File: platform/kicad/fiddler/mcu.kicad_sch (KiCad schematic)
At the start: 9 parts, among them SW1 SW_Push, SW2 SW_Push, U1 ESP32-WROOM-32E

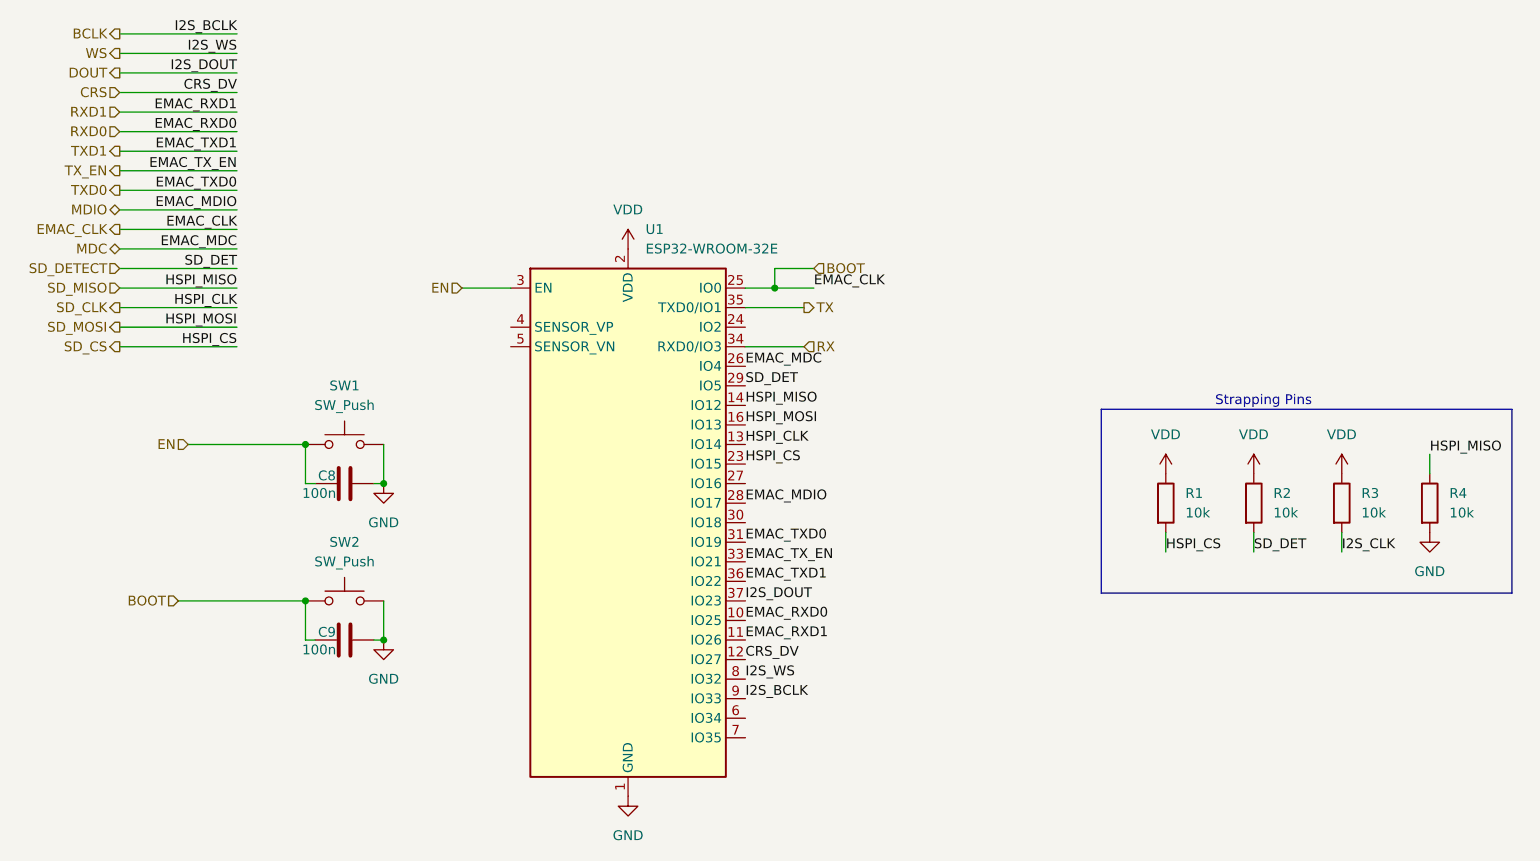
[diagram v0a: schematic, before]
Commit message: Fiddler Ray Speaker: Complete first revision
This change completes the first iteration schematic and layout for the fiddler ray speaker PCB.
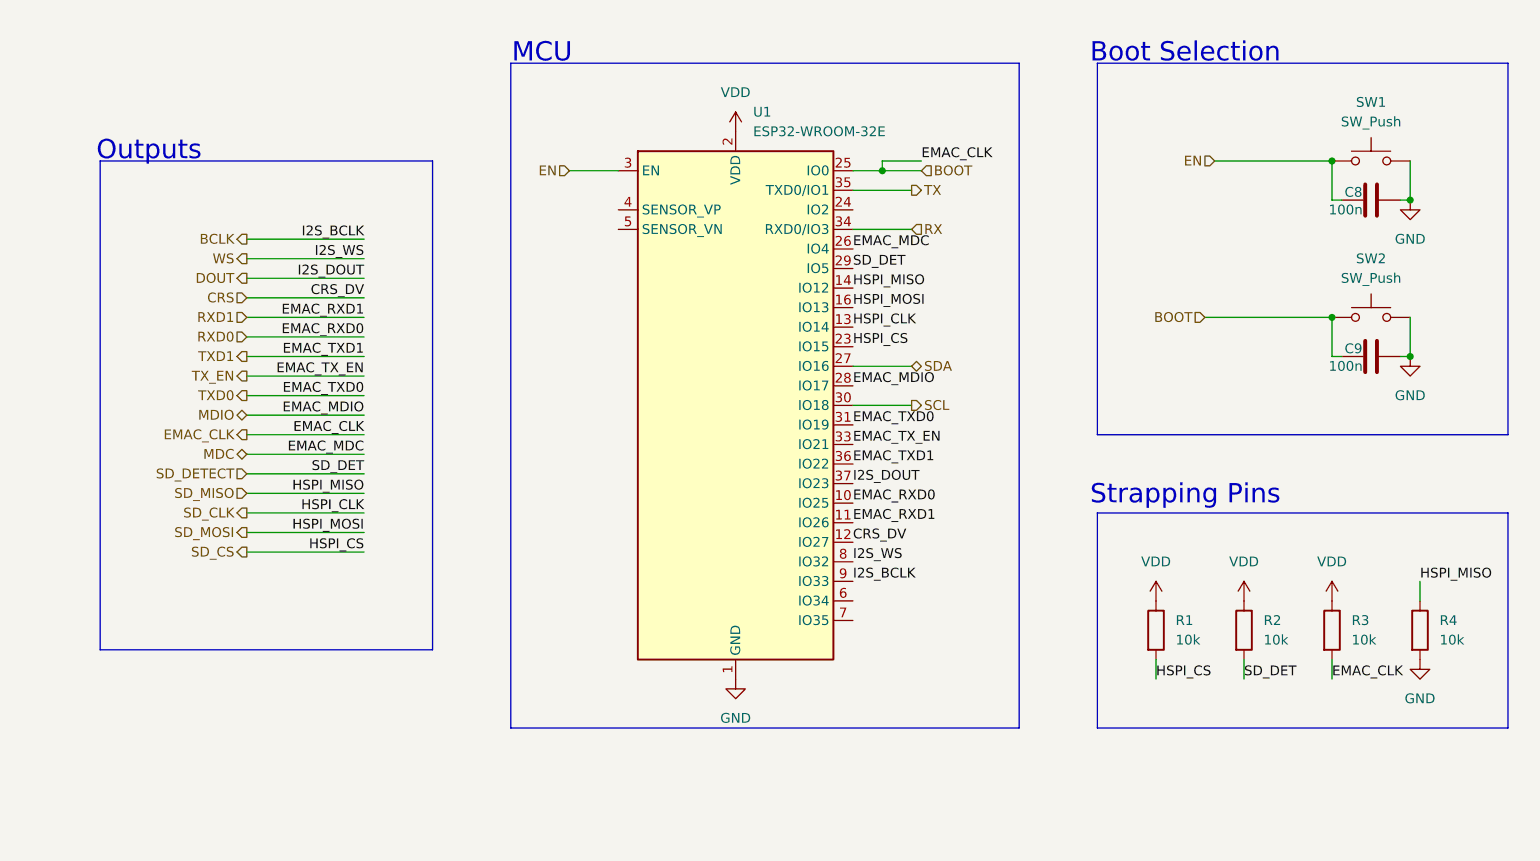
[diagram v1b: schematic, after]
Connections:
- net I2S_CLK is gone; now on net BOOT: R3.2
- net SDA: now reaches U1.27 (IO16)
- net SCL: now reaches U1.30 (IO18)
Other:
- note added: "Boot Selection"
- note added: "MCU"
- note added: "Outputs"
- company: (none) -> The Australian Ocean Laboratory
- title: (none) -> Fiddler Ray Speaker Unit V1
- moved on the sheet: C8, C9, R1, R2, R3, R4, SW1, SW2, U1

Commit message: Fiddler Ray Speaker: Production rev A
This change adds additional data to components to populate SPN for
the BOM via JLC
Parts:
- C8, C9: LCSC Part # (none) -> C14663
- SW1, SW2: footprint Resistor_SMD:R_0603_1608Metric -> AusOcean:SW_B3U-1000P; LCSC Part # (none) -> C720477
- U1: LCSC Part # (none) -> C701341
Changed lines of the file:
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@@
+			)
+		)
+		(property "Voltage Rating" ""
+			(at 229.87 124.46 0)
+			(effects
+				(font
+					(size 1.27 1.27)
+				)
+				(hide yes)
+			)
+		)
+		(property "LCSC Part #" ""
+			(at 229.87 124.46 0)
+			(effects
+				(font
+					(size 1.27 1.27)
+				)
+				(hide yes)
 			)
 		)
@@
 		(property "Description" "Unpolarized capacitor"
 			(at 223.52 68.58 0)
+			(effects
+				(font
+					(size 1.27 1.27)
+				)
+				(hide yes)
+			)
+		)
+		(property "Voltage Rating" ""
+			(at 223.52 68.58 90)
+			(effects
+				(font
+					(size 1.27 1.27)
+				)
+				(hide yes)
+			)
+		)
+		(property "LCSC Part #" "C14663"
+			(at 223.52 68.58 90)
 			(effects
 				(font
@@
 			)
 		)
-		(property "Footprint" "Resistor_SMD:R_0603_1608Metric"
+		(property "Footprint" "AusOcean:SW_B3U-1000P"
 			(at 223.52 78.74 0)
 			(effects
@@
 			)
 		)
+		(property "Voltage Rating" ""
+			(at 223.52 83.82 0)
+			(effects
+				(font
+					(size 1.27 1.27)
+				)
+				(hide yes)
+			)
+		)
+		(property "LCSC Part #" "C720477"
+			(at 223.52 83.82 0)
+			(effects
+				(font
+					(size 1.27 1.27)
+				)
+				(hide yes)
+			)
+		)
 		(pin "2"
 		)
@@
 		(property "Description" "Unpolarized capacitor"
 			(at 223.52 88.9 0)
+			(effects
+				(font
+					(size 1.27 1.27)
+				)
+				(hide yes)
+			)
+		)
+		(property "Voltage Rating" ""
+			(at 223.52 88.9 90)
+			(effects
+				(font
+					(size 1.27 1.27)
+				)
+				(hide yes)
+			)
+		)
+		(property "LCSC Part #" "C14663"
+			(at 223.52 88.9 90)
 			(effects
 				(font
@@
 			)
 		)
-		(property "Footprint" "Resistor_SMD:R_0603_1608Metric"
+		(property "Footprint" "AusOcean:SW_B3U-1000P"
 			(at 223.52 58.42 0)
 			(effects
@@
 		)
 		(property "Description" "Push button switch, generic, two pins"
+			(at 223.52 63.5 0)
+			(effects
+				(font
+					(size 1.27 1.27)
+				)
+				(hide yes)
+			)
+		)
+		(property "Voltage Rating" ""
+			(at 223.52 63.5 0)
+			(effects
+				(font
+					(size 1.27 1.27)
+				)
+				(hide yes)
+			)
+		)
+		(property "LCSC Part #" "C720477"
 			(at 223.52 63.5 0)
 			(effects
@@
 			)
 		)
+		(property "Voltage Rating" ""
+			(at 218.44 124.46 0)
+			(effects
+				(font
+					(size 1.27 1.27)
+				)
+				(hide yes)
+			)
+		)
+		(property "LCSC Part #" ""
+			(at 218.44 124.46 0)
+			(effects
+				(font
+					(size 1.27 1.27)
+				)
+				(hide yes)
+			)
+		)
 		(pin "1"
 		)
@@
 			)
 		)
+		(property "Voltage Rating" ""
+			(at 140.97 95.25 0)
+			(effects
+				(font
+					(size 1.27 1.27)
+				)
+				(hide yes)
+			)
+		)
+		(property "LCSC Part #" "C701341"
+			(at 140.97 95.25 0)
+			(effects
+				(font
+					(size 1.27 1.27)
+				)
+				(hide yes)
+			)
+		)
 		(pin "26"
 		)
@@
 			)
 		)
+		(property "Voltage Rating" ""
+			(at 207.01 124.46 0)
+			(effects
+				(font
+					(size 1.27 1.27)
+				)
+				(hide yes)
+			)
+		)
+		(property "LCSC Part #" ""
+			(at 207.01 124.46 0)
+			(effects
+				(font
+					(size 1.27 1.27)
+				)
+				(hide yes)
+			)
+		)
 		(pin "1"
 		)
@@
 			(at 195.58 124.46 0)
 			(effects
+				(font
+					(size 1.27 1.27)
+				)
+				(hide yes)
+			)
+		)
+		(property "Voltage Rating" ""
+			(at 195.58 124.46 0)
+			(effects
+				(font
+					(size 1.27 1.27)
+				)
+				(hide yes)
+			)
+		)
+		(property "LCSC Part #" ""
+			(at 195.58 124.46 0)
+			(effects
